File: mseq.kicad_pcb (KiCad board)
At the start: 2 copper layers, 135.3 x 78.4 mm, 93 parts, among them J1 Screen_I2C, J3 Conn_ARM_JTAG_SWD_10, SW1 RESET, SW2 ON/OFF, SW3 MS/SLAVE, SW4 BOOT, U1 SN74HCT125DR, U2 H11L1M, U3 AMS1117-3.3, U4 STM32F413CHUx, U5 CP2102N-Axx-xQFN20, U6 H11L1M, U7 W25Q16JVSS, U8 MB85RS256B, Y1 32.768kHz ±20ppm 6pF, Y2 25 MHz ±20ppm 18pF

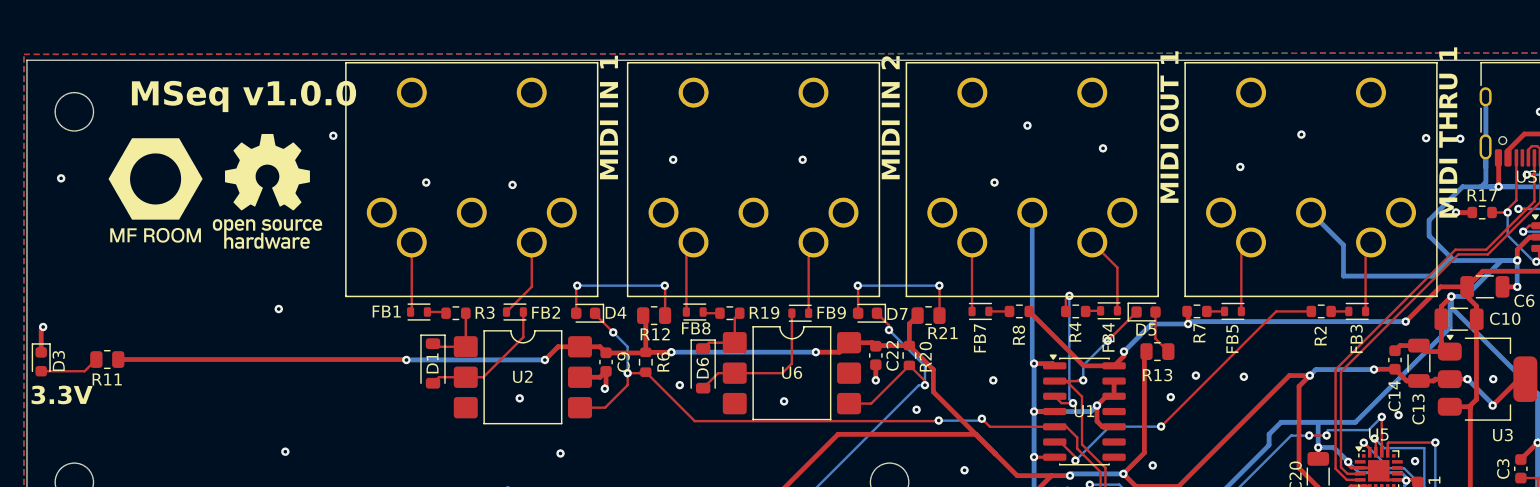
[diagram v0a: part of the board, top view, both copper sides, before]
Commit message: Fix DIN-504 footprint pin rows, restore MIDI references, clean fp-lib-table
- DIN-504: pins 4/5 moved from 2.49 mm to 2.1 mm behind pins 1/2/3 (LCSC
  datasheet for C23689428); updated in the library and on the board
- DIN footprints use their schematic references (MIDI_IN1 ...) again; the
  front-panel labels are now free silkscreen text, so BOM/CPL designators
  are clean and Update-PCB-from-Schematic no longer renames them
- TXT/RXT labels: trailing newline removed
- fp-lib-table: dropped a dangling "fps" entry and a duplicated mseq_lib line

Co-Authored-By: Claude Fable 5.1 <noreply@anthropic.com>
Claude-Session: https://claude.ai/code/session_014D6qtQcTakGg9PCa4hkr3z
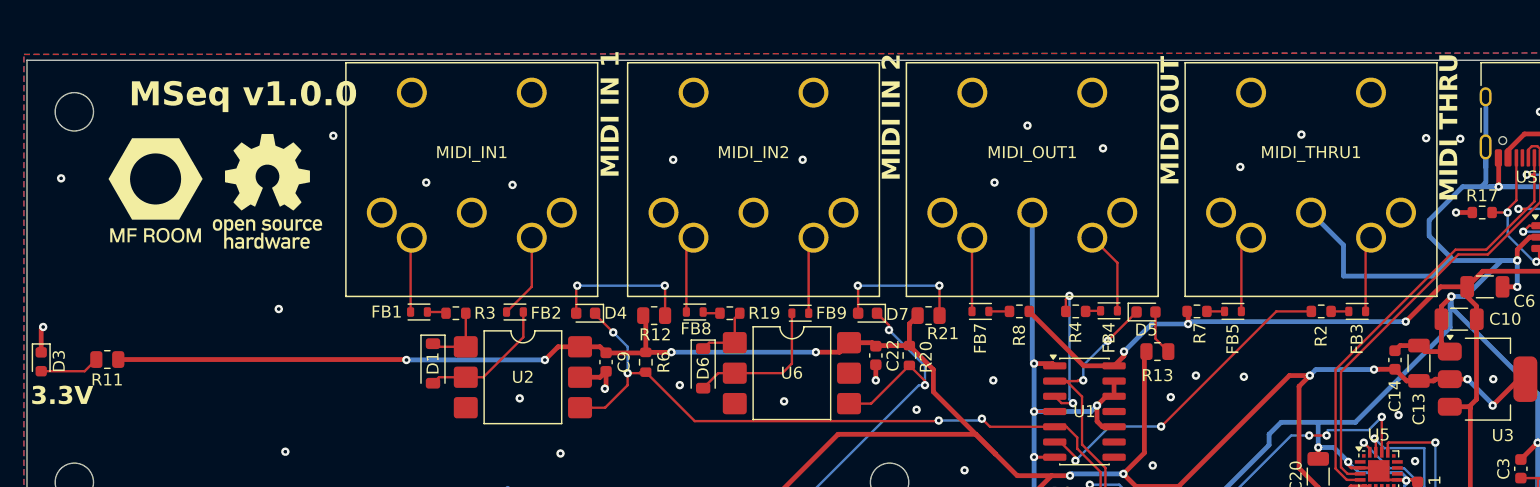
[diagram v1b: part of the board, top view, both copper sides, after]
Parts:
- MIDI_IN1: renamed from MIDI IN 1
- MIDI_IN2: renamed from MIDI IN 2
- MIDI_OUT1: renamed from MIDI OUT 1
- MIDI_THRU1: renamed from MIDI THRU 1
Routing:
- net Net-(FB8-Pad2): track 6.05 -> 7.29 mm
- net Net-(FB3-Pad1): track 5.94 -> 6.98 mm
- net Net-(FB9-Pad2): track 6.07 -> 7.04 mm
- net Net-(FB1-Pad2): track 5.90 -> 6.44 mm
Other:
- board text added: "MIDI IN 1"
- board text added: "MIDI IN 2"
- board text added: "MIDI OUT"
- board text added: "MIDI THRU"
